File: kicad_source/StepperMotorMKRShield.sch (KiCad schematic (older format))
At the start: 15 parts, among them CN1 ADAFRUIT_FEATHER, CN2 DNI, CN3 BM04B-SRSS-TB, CN4 CONN_01X04, Y1 ECS-3225MV-160-BN-TR

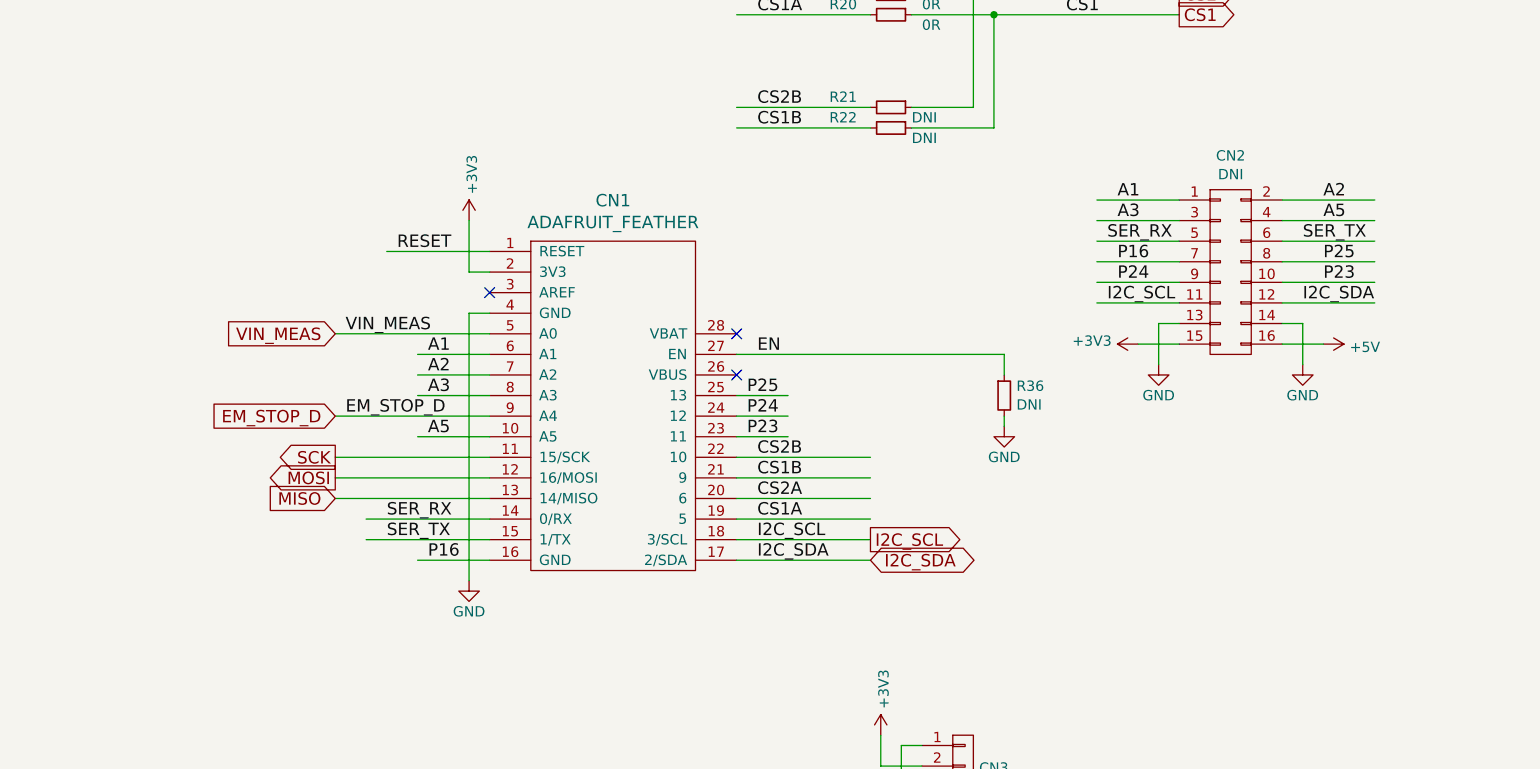
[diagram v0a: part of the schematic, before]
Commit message: added CN1 from adafruit feather to arduino MKR
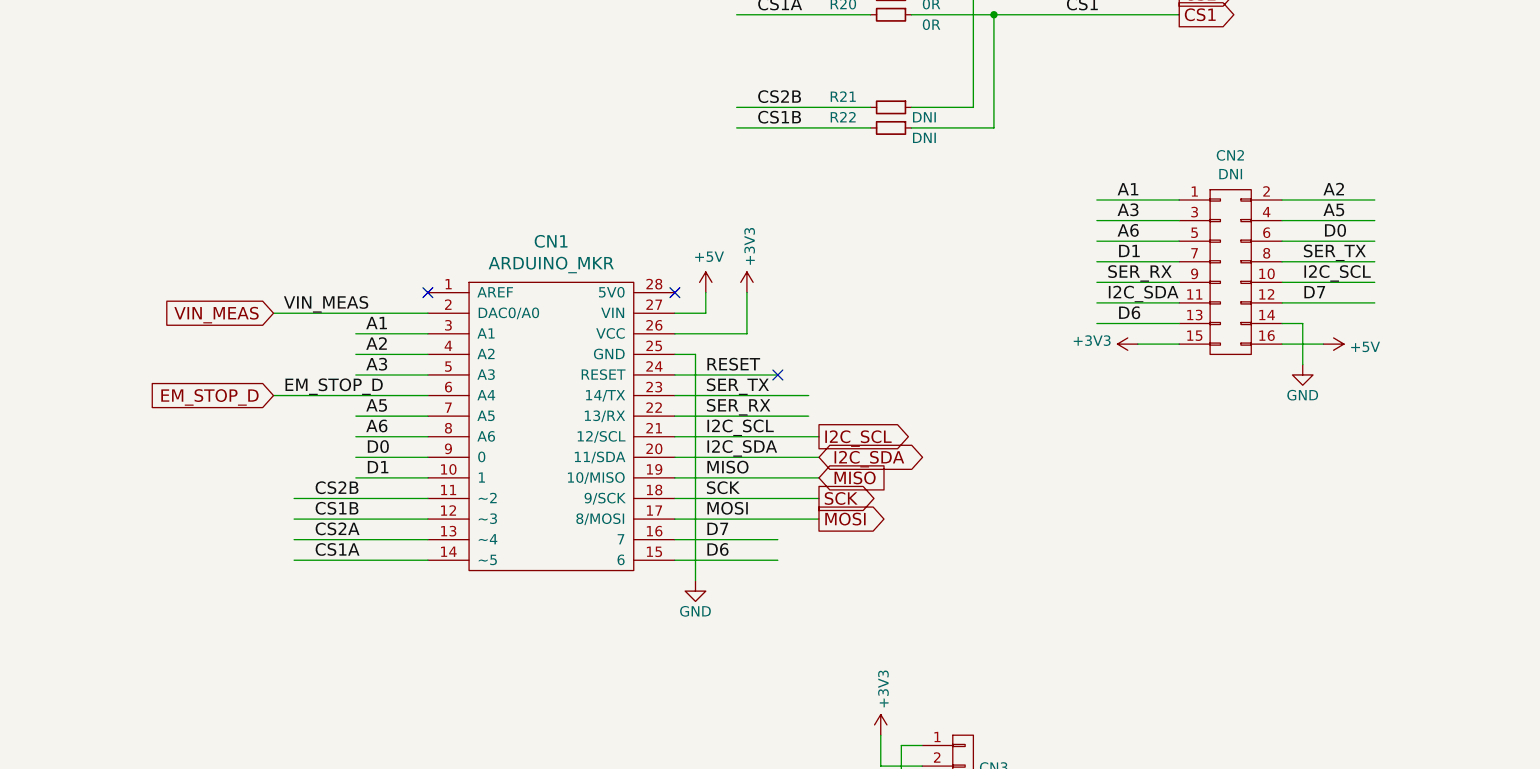
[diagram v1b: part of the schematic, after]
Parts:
- removed CN1: ADAFRUIT_FEATHER, MODULE_compute:ADAFRUIT_FEATHER_HOLES, symbol MODULE_compute:ADAFRUIT_FEATHER
- removed R36: DNI, resistors:R_0603, symbol devices:R_0603
- added CN1: ARDUINO_MKR, MODULE_compute:ARDUINO_MKR, symbol MODULE_compute:ARDUINO_MKR
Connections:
- net labels added: A6, D0, D1, D6, D7
- net labels removed: EN, P16, P23, P24, P25
- wire segments 80 -> 79

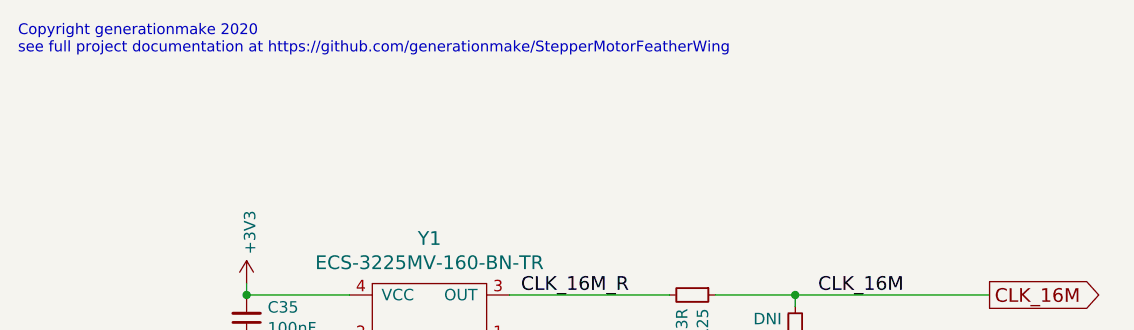
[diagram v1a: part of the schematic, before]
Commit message: corrected links and titles, generated schematic pdf and net list
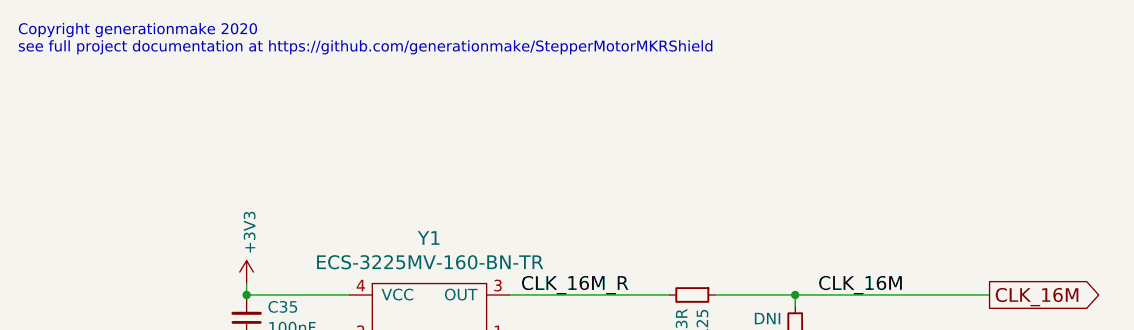
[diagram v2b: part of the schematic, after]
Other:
- note added: "Copyright generationmake 2020\nsee full project documentation at https://github.com/generationmake/StepperMotorMKRShield"
- note removed: "Copyright generationmake 2020\nsee full project documentation at https://github.com/generationmake/StepperMotorFeatherWing"
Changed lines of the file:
@@
 encoding utf-8
 Sheet 1 6
-Title "StepperMotorFeatherWing"
-Date "2020-07-11"
-Rev "1.1"
+Title "StepperMotorMKRShield"
+Date "2020-07-12"
+Rev "1.0"
 Comp "generationmake"
 Comment1 ""
@@
 $EndDescr
 Text Notes 500  650  0    47   ~ 0
-Copyright generationmake 2020\nsee full project documentation at https://github.com/generationmake/StepperMotorFeatherWing
+Copyright generationmake 2020\nsee full project documentation at https://github.com/generationmake/StepperMotorMKRShield
 Text Notes 7000 6900 0    43   ~ 0
 You may redistribute and modify this documentation under the terms of the CERN OHL v.1.2. (http://ohwr.org/cernohl). \nThis documentation is distributed WITHOUT ANY EXPRESS OR IMPLIED WARRANTY, INCLUDING OF MERCHANTABILITY, SATISFACTORY \nQUALITY AND FITNESS FOR A PARTICULAR PURPOSE. Please see the CERN OHL v.1.2  for applicable conditions
@@
 NoConn ~ 3700 3950
 $Comp
-L power-supply:+5V #PWR?
+L power-supply:+5V #PWR0105
 U 1 1 5F0BADF9
 P 3850 3950
-F 0 "#PWR?" H 3850 3800 50  0001 C CNN
+F 0 "#PWR0105" H 3850 3800 50  0001 C CNN
 F 1 "+5V" H 3865 4123 50  0000 C CNN
 F 2 "" H 3850 3950 50  0000 C CNN
@@
 $EndComp
 $Comp
-L power-supply:GND #PWR?
+L power-supply:GND #PWR0113
 U 1 1 5F0BB92C
 P 3800 5350
-F 0 "#PWR?" H 3800 5100 50  0001 C CNN
+F 0 "#PWR0113" H 3800 5100 50  0001 C CNN
 F 1 "GND" H 3800 5200 50  0000 C CNN
 F 2 "" H 3800 5350 50  0000 C CNN

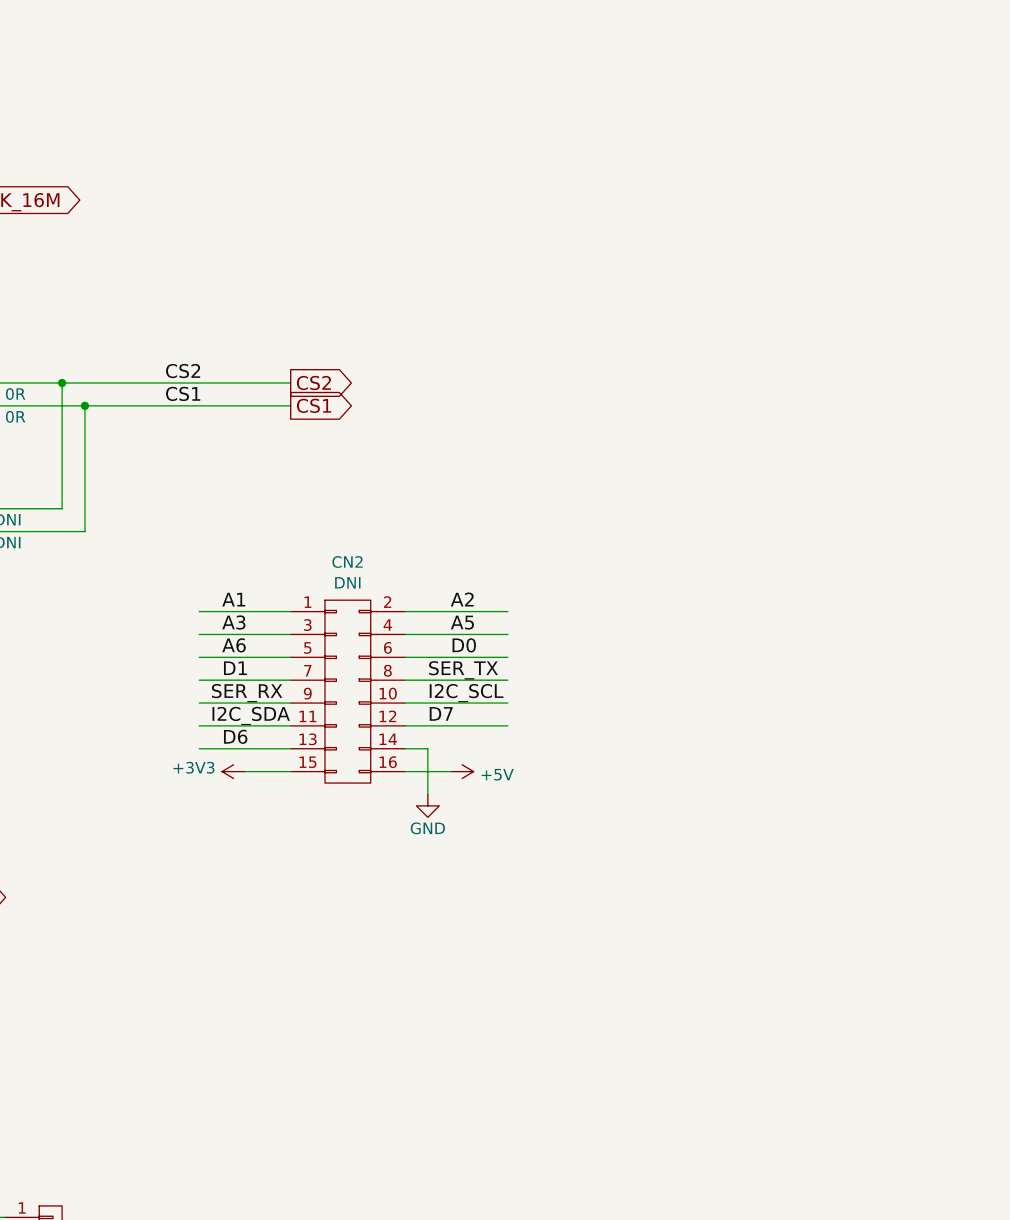
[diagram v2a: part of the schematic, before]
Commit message: added Arduino Nano 33 header in schematic
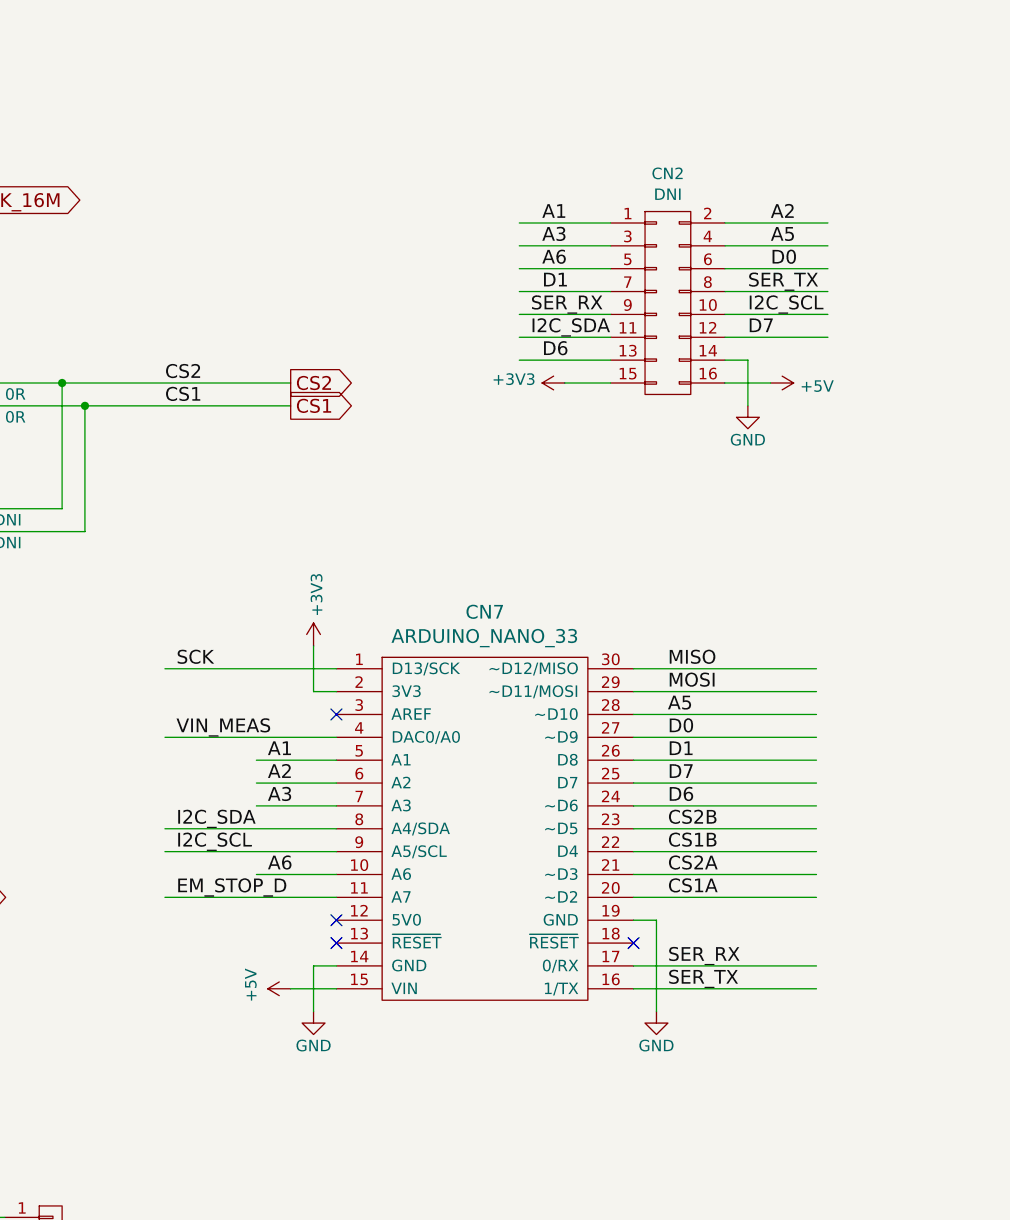
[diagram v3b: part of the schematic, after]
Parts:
- added CN7: ARDUINO_NANO_33, MODULE_compute:ARDUINO_NANO_33, symbol MODULE_compute:ARDUINO_NANO_33
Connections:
- wire segments 79 -> 108
- no-connect marks 4 -> 8
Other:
- moved on the sheet: CN2

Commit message: updated layout
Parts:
- CN1: footprint MODULE_compute:ARDUINO_MKR -> MODULE_compute:ARDUINO_MKR_BASEBOARD
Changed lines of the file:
@@
 F 0 "CN1" H 3100 5497 60  0000 C CNN
 F 1 "ARDUINO_MKR" H 3100 5391 60  0000 C CNN
-F 2 "MODULE_compute:ARDUINO_MKR" H 3000 5250 60  0001 C CNN
+F 2 "MODULE_compute:ARDUINO_MKR_BASEBOARD" H 3000 5250 60  0001 C CNN
 F 3 "" H 3100 4300 60  0000 C CNN
 	1    3100 4600
